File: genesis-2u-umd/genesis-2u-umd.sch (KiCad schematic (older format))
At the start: 4 parts

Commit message: working on schematic
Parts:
- removed CON? (x2): UMD-CONN, db-thparts:UMD-CONN-DIP64, symbol UMD-CONN
- added CON? (x2): UMDv2-CONN, db-thparts:UMD-CONN-DIP64, symbol UMDv2-CONN
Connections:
- net labels added: +5V, A1, A10, A11, A12, A13, A14, A15, A16, A17, A18, A19, A2, A20, A21, A22, A23, A3, A4, A5, A6, A7, A8, A9, D0, D1, D10, D11, D12, D13, D14, D15, D2, D3, D4, D5, D6, D7, D8, D9, GND, ~CART~, ~CE0~, ~CE1~, ~LWR~, ~M3~, ~OE­~, ~RST~, ~TIME~, ~UWR~
- wire segments 0 -> 106
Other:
- moved on the sheet: CON?

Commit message: more work on schematic
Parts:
- added U? (x2): MCP23008T-E/SO, db-smt:SOIC-18, symbol MCP23008T-E/SO
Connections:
- net labels added: +3V3, A0, SCL, SDA, ~RD~, ~WR~
- wire segments 106 -> 180
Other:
- moved on the sheet: CON?A, CON?B

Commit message: working on schematic
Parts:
- added C?: 0.1uF/50V, db-smt:0603, symbol C_0603
- added C?: 10uF/10V, db-smt:0805, symbol C_0805
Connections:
- wire segments 180 -> 188
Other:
- moved on the sheet: U?A, U?B
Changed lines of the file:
@@
 Comment1 "Licensed Under CERN OHL v.1.2"
 Comment2 "https://github.com/db-electronics/umd-genesis-adapter-kicad"
-Comment3 ""
+Comment3 "Copyright René Richard"
 Comment4 ""
 $EndDescr
@@
 L MCP23008T-E/SO U?
 U 1 1 5B909634
-P 3300 6200
-F 0 "U?" H 3525 6350 50  0000 C CNN
-F 1 "MCP23008T-E/SO" H 3800 6250 50  0000 C CNN
-F 2 "db-smt:SOIC-18" H 3775 6900 60  0001 C CNN
-F 3 "http://ww1.microchip.com/downloads/en/DeviceDoc/21919e.pdf" H 4750 6800 60  0001 C CNN
-F 4 "MCP23008T-E/SOCT-ND" H 4000 6700 60  0001 C CNN "Digikey"
-F 5 "IC I/O EXPANDER I2C 8B 18SOIC" H 4150 6600 60  0001 C CNN "Description"
-	1    3300 6200
+P 4625 6200
+F 0 "U?" H 4700 6350 50  0000 C CNN
+F 1 "MCP23008T-E/SO" H 4975 6250 50  0000 C CNN
+F 2 "db-smt:SOIC-18" H 5100 6900 60  0001 C CNN
+F 3 "http://ww1.microchip.com/downloads/en/DeviceDoc/21919e.pdf" H 6075 6800 60  0001 C CNN
+F 4 "MCP23008T-E/SOCT-ND" H 5325 6700 60  0001 C CNN "Digikey"
+F 5 "IC I/O EXPANDER I2C 8B 18SOIC" H 5475 6600 60  0001 C CNN "Description"
+	1    4625 6200
 	1    0    0    -1
 $EndComp
@@
 L MCP23008T-E/SO U?
 U 2 1 5B90968F
-P 1250 6400
-F 0 "U?" H 1475 6550 50  0000 C CNN
-F 1 "MCP23008T-E/SO" H 1750 6450 50  0000 C CNN
-F 2 "db-smt:SOIC-18" H 1725 7100 60  0001 C CNN
-F 3 "http://ww1.microchip.com/downloads/en/DeviceDoc/21919e.pdf" H 2700 7000 60  0001 C CNN
-F 4 "MCP23008T-E/SOCT-ND" H 1950 6900 60  0001 C CNN "Digikey"
-F 5 "IC I/O EXPANDER I2C 8B 18SOIC" H 2100 6800 60  0001 C CNN "Description"
-	2    1250 6400
+P 2825 6425
+F 0 "U?" H 3025 6575 50  0000 C CNN
+F 1 "MCP23008T-E/SO" H 3300 6475 50  0000 C CNN
+F 2 "db-smt:SOIC-18" H 3300 7125 60  0001 C CNN
+F 3 "http://ww1.microchip.com/downloads/en/DeviceDoc/21919e.pdf" H 4275 7025 60  0001 C CNN
+F 4 "MCP23008T-E/SOCT-ND" H 3525 6925 60  0001 C CNN "Digikey"
+F 5 "IC I/O EXPANDER I2C 8B 18SOIC" H 3675 6825 60  0001 C CNN "Description"
+	2    2825 6425
 	1    0    0    -1
 $EndComp
@@
 L GND #PWR?
 U 1 1 5B9099C4
-P 1350 7150
-F 0 "#PWR?" H 1350 6900 50  0001 C CNN
-F 1 "GND" H 1350 7000 50  0000 C CNN
-F 2 "" H 1350 7150 50  0000 C CNN
-F 3 "" H 1350 7150 50  0000 C CNN
-	1    1350 7150
+P 2925 7175
+F 0 "#PWR?" H 2925 6925 50  0001 C CNN
+F 1 "GND" H 2925 7025 50  0000 C CNN
+F 2 "" H 2925 7175 50  0000 C CNN
+F 3 "" H 2925 7175 50  0000 C CNN
+	1    2925 7175
 	1    0    0    -1
 $EndComp
@@
 L +3V3 #PWR?
 U 1 1 5B909A1D
-P 1350 6100
-F 0 "#PWR?" H 1350 5950 50  0001 C CNN
-F 1 "+3V3" H 1350 6240 50  0000 C CNN
-F 2 "" H 1350 6100 50  0000 C CNN
-F 3 "" H 1350 6100 50  0000 C CNN
-	1    1350 6100
-	1    0    0    -1
-$EndComp
-Wire Wire Line
-	1350 7050 1350 7150
-Wire Wire Line
-	1350 6100 1350 6200
+P 2925 6125
+F 0 "#PWR?" H 2925 5975 50  0001 C CNN
+F 1 "+3V3" H 2925 6265 50  0000 C CNN
+F 2 "" H 2925 6125 50  0000 C CNN
+F 3 "" H 2925 6125 50  0000 C CNN
+	1    2925 6125
+	1    0    0    -1
+$EndComp
+Wire Wire Line
+	2925 7075 2925 7175
+Wire Wire Line
+	2925 6125 2925 6225
 Wire Wire Line
 	3950 2450 3400 2450
@@
 SDA
 Wire Wire Line
-	3100 6400 2550 6400
-Text Label 2600 6300 0    60   ~ 0
+	4425 6400 3875 6400
+Text Label 3925 6300 0    60   ~ 0
 SCL
 Wire Wire Line
-	3100 6300 2550 6300
-Text Label 2600 6400 0    60   ~ 0
+	4425 6300 3875 6300
+Text Label 3925 6400 0    60   ~ 0
 SDA
 $Comp
 L GND #PWR?
 U 1 1 5B90A027
-P 3000 7200
-F 0 "#PWR?" H 3000 6950 50  0001 C CNN
-F 1 "GND" H 3000 7050 50  0000 C CNN
-F 2 "" H 3000 7200 50  0000 C CNN
-F 3 "" H 3000 7200 50  0000 C CNN
-	1    3000 7200
-	1    0    0    -1
-$EndComp
-Wire Wire Line
-	3100 6600 3000 6600
-Wire Wire Line
-	3000 6600 3000 7200
-Wire Wire Line
-	3100 6700 3000 6700
-Connection ~ 3000 6700
-Wire Wire Line
-	3100 6800 3000 6800
-Connection ~ 3000 6800
+P 4325 7200
+F 0 "#PWR?" H 4325 6950 50  0001 C CNN
+F 1 "GND" H 4325 7050 50  0000 C CNN
+F 2 "" H 4325 7200 50  0000 C CNN
+F 3 "" H 4325 7200 50  0000 C CNN
+	1    4325 7200
+	1    0    0    -1
+$EndComp
+Wire Wire Line
+	4425 6600 4325 6600
+Wire Wire Line
+	4325 6600 4325 7200
+Wire Wire Line
+	4425 6700 4325 6700
+Connection ~ 4325 6700
+Wire Wire Line
+	4425 6800 4325 6800
+Connection ~ 4325 6800
 $Comp
 L GND #PWR?
 U 1 1 5B90A3C2
-P 4250 7200
-F 0 "#PWR?" H 4250 6950 50  0001 C CNN
-F 1 "GND" H 4250 7050 50  0000 C CNN
-F 2 "" H 4250 7200 50  0000 C CNN
-F 3 "" H 4250 7200 50  0000 C CNN
-	1    4250 7200
+P 5575 7200
+F 0 "#PWR?" H 5575 6950 50  0001 C CNN
+F 1 "GND" H 5575 7050 50  0000 C CNN
+F 2 "" H 5575 7200 50  0000 C CNN
+F 3 "" H 5575 7200 50  0000 C CNN
+	1    5575 7200
 	1    0    0    -1
 $EndComp
@@
 L +3V3 #PWR?
 U 1 1 5B90A3DF
-P 4250 6200
-F 0 "#PWR?" H 4250 6050 50  0001 C CNN
-F 1 "+3V3" H 4250 6340 50  0000 C CNN
-F 2 "" H 4250 6200 50  0000 C CNN
-F 3 "" H 4250 6200 50  0000 C CNN
-	1    4250 6200
-	1    0    0    -1
-$EndComp
-Wire Wire Line
-	4150 6300 4250 6300
-Wire Wire Line
-	4250 6300 4250 6200
-Wire Wire Line
-	4150 6400 4250 6400
-Wire Wire Line
-	4250 6400 4250 7200
-Wire Wire Line
-	4150 6500 4250 6500
-Connection ~ 4250 6500
-Wire Wire Line
-	4150 6600 4250 6600
-Connection ~ 4250 6600
-Wire Wire Line
-	4150 6700 4250 6700
-Connection ~ 4250 6700
-Wire Wire Line
-	4150 6800 4250 6800
-Connection ~ 4250 6800
-Wire Wire Line
-	4150 6900 4250 6900
-Connection ~ 4250 6900
-Wire Wire Line
-	4150 7000 4250 7000
-Connection ~ 4250 7000
+P 5575 6200
+F 0 "#PWR?" H 5575 6050 50  0001 C CNN
+F 1 "+3V3" H 5575 6340 50  0000 C CNN
+F 2 "" H 5575 6200 50  0000 C CNN
+F 3 "" H 5575 6200 50  0000 C CNN
+	1    5575 6200
+	1    0    0    -1
+$EndComp
+Wire Wire Line
+	5475 6300 5575 6300
+Wire Wire Line
+	5575 6300 5575 6200
+Wire Wire Line
+	5475 6400 5575 6400
+Wire Wire Line
+	5575 6400 5575 7200
+Wire Wire Line
+	5475 6500 5575 6500
+Connection ~ 5575 6500
+Wire Wire Line
+	5475 6600 5575 6600
+Connection ~ 5575 6600
+Wire Wire Line
+	5475 6700 5575 6700
+Connection ~ 5575 6700
+Wire Wire Line
+	5475 6800 5575 6800
+Connection ~ 5575 6800
+Wire Wire Line
+	5475 6900 5575 6900
+Connection ~ 5575 6900
+Wire Wire Line
+	5475 7000 5575 7000
+Connection ~ 5575 7000
+Wire Wire Line
+	3950 2850 3400 2850
+Text Label 3450 2850 0    60   ~ 0
+~TIME~
+$Comp
+L C_0603 C?
+U 1 1 5B915F2C
+P 2375 6650
+F 0 "C?" H 2400 6750 50  0000 L CNN
+F 1 "0.1uF/50V" H 2400 6550 50  0000 L CNN
+F 2 "db-smt:0603" H 2875 6550 30  0001 C CNN
+F 3 "" H 2400 6750 60  0001 C CNN
+F 4 "490-8020-1-ND" H 2800 6625 60  0001 C CNN "Digikey"
+F 5 "CAP CER 0.1UF 50V X7R 0603" H 2800 6725 60  0001 C CNN "Description"
+	1    2375 6650
+	1    0    0    -1
+$EndComp
+Wire Wire Line
+	1850 6175 2925 6175
+Wire Wire Line
+	2375 6175 2375 6500
+Connection ~ 2925 6175
+Wire Wire Line
+	2375 6800 2375 7125
+Wire Wire Line
+	1850 7125 2925 7125
+Connection ~ 2925 7125
+Wire Wire Line
+	3950 2750 3400 2750
+Text Label 3450 2750 0    60   ~ 0
+~LWR~
+$Comp
+L C_0805 C?
+U 1 1 5B916B80
+P 1850 6650
+F 0 "C?" H 1875 6750 50  0000 L CNN
+F 1 "10uF/10V" H 1875 6550 50  0000 L CNN
+F 2 "db-smt:0805" H 1888 6500 30  0001 C CNN
+F 3 "" H 1875 6750 60  0000 C CNN
+F 4 "1276-2934-1-ND" H 1975 6850 60  0001 C CNN "Digikey"
+F 5 "CAP CER 10UF 10V X7R 0805" H 1975 6950 60  0001 C CNN "Description"
+	1    1850 6650
+	1    0    0    -1
+$EndComp
+Wire Wire Line
+	1850 6500 1850 6175
+Connection ~ 2375 6175
+Wire Wire Line
+	1850 6800 1850 7125
+Connection ~ 2375 7125
 $EndSCHEMATC

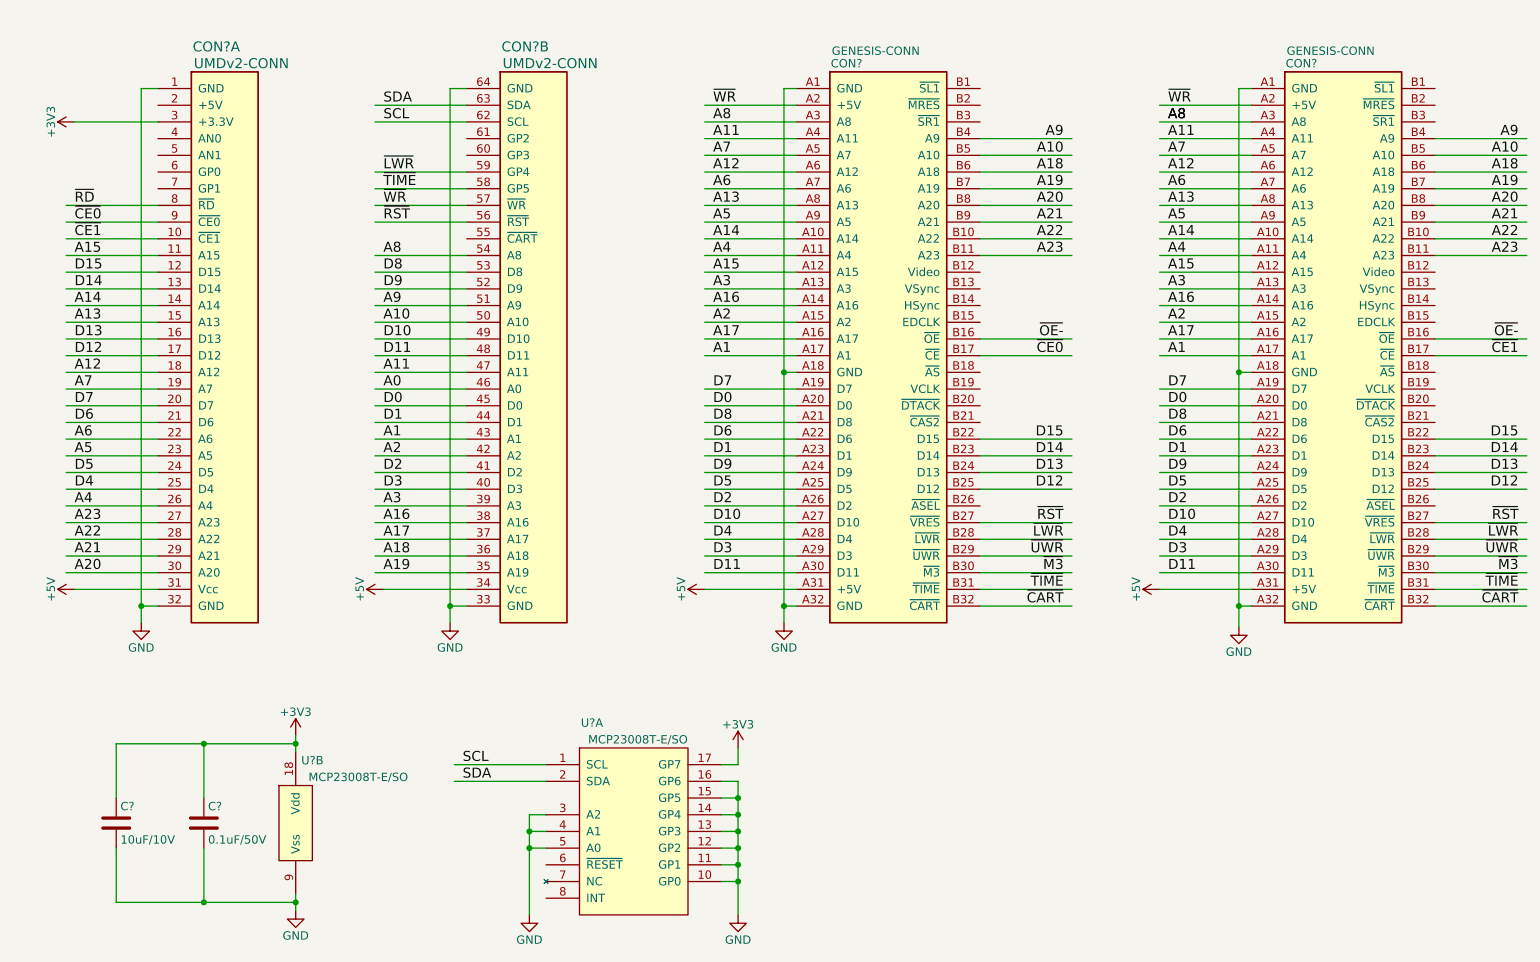
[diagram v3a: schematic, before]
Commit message: split TIME into two signals for dual cart
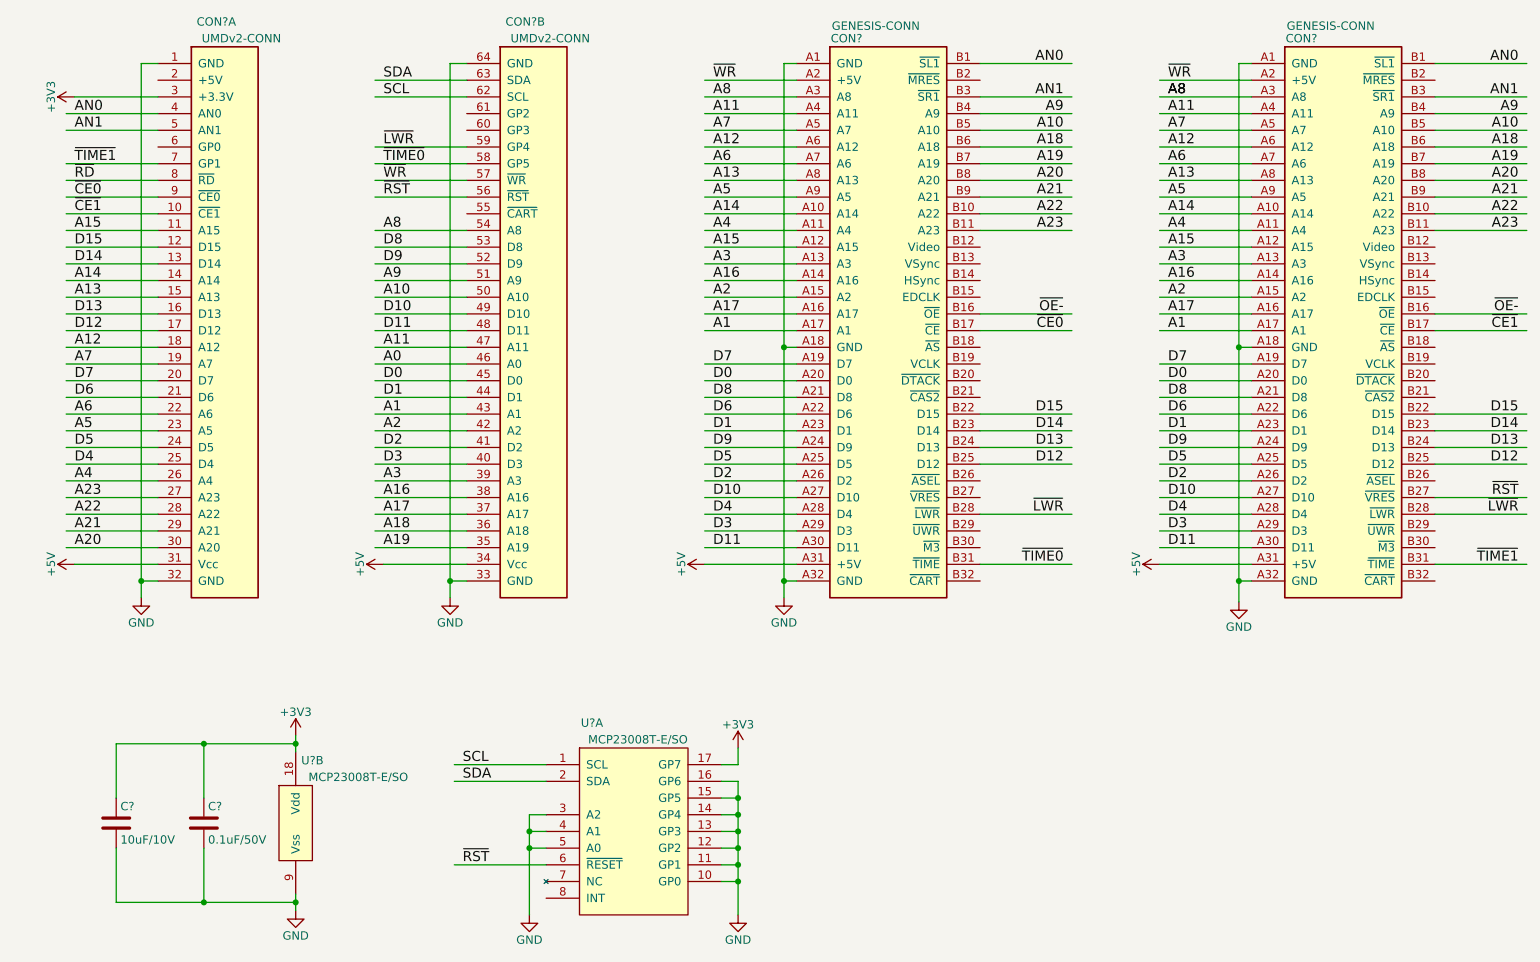
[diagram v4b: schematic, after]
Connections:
- net labels added: AN0, AN1, ~TIME0~, ~TIME1~
- net labels removed: ~CART~, ~M3~, ~TIME~, ~UWR~
- wire segments 188 -> 207
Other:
- moved on the sheet: CON?, CON?A, CON?B
